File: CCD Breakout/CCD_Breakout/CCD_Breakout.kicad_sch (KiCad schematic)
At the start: 11 parts, among them Q1 PNP, U1 ILX511

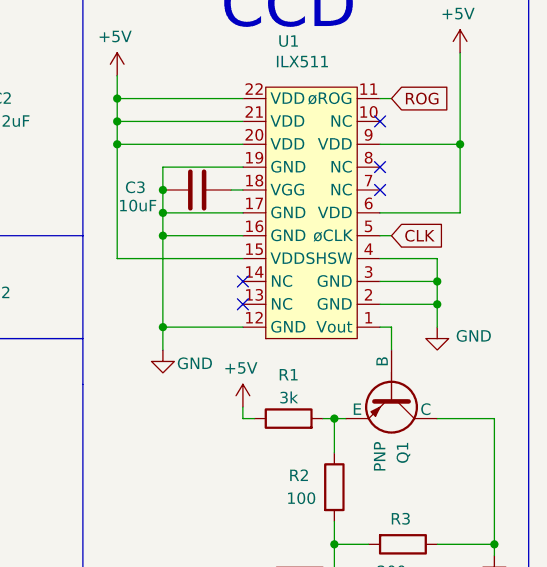
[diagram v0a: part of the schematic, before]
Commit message: Updated CCD SHSW as well as the pin connector between both boards. Still need to adjust an even frame size, adjust length of ethernet cables, generate GERBS, and check all input/output flags, as well as GND field. May have forgotten something
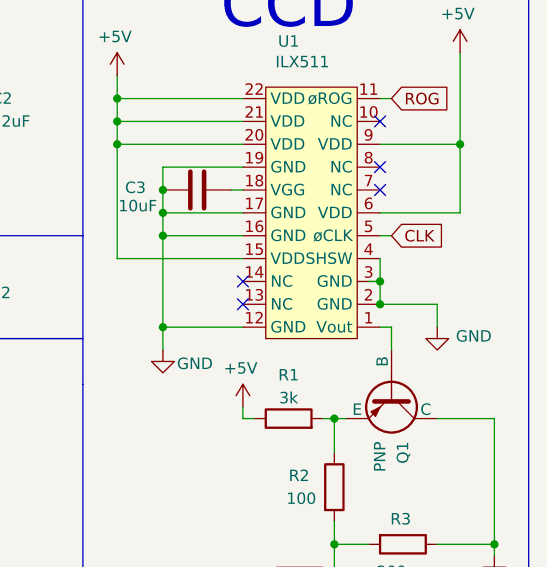
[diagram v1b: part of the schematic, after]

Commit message: Fixed bjt and SL on CCD Breakout
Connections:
- net GND: now also Q1.3 (C); no longer Q1.1 (C)
- net at U1.1 (Vout): now also Q1.1 (B); no longer Q1.2 (B)
- net at R1.2, R2.1: now also Q1.2 (E); no longer Q1.3 (E)
